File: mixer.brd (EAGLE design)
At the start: 23 x 40 mm, 21 parts, among them U2 SA602AD8-SOIC

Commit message: updating layouts and parts
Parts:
- moved JP1 0.64 mm to (11.5, 3.17)
- moved R4 0.25 mm to (1.91, 7.11)
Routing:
- net GND: track 117.4 -> 0.00 mm
- net N$5: track 56.3 -> 35.7 mm, vias 0 -> 1
- net ANT_OUT: track 42.9 -> 29.7 mm, vias 1 -> 0
- net N$1: track 6.50 -> 17.9 mm
- net N$2: track 7.98 -> 17.6 mm
- net OUT_A: track 14.4 -> 18.6 mm, vias 0 -> 1
- net N$4: track 13.6 -> 15.3 mm, vias 0 -> 1
- net N$16: track 19.8 -> 21.5 mm, vias 2 -> 0
- net 6V_DC: track 27.5 -> 28.7 mm
- net ANT_IN: track 22.3 -> 23.5 mm
- net OUT_B: track 13.1 -> 12.3 mm

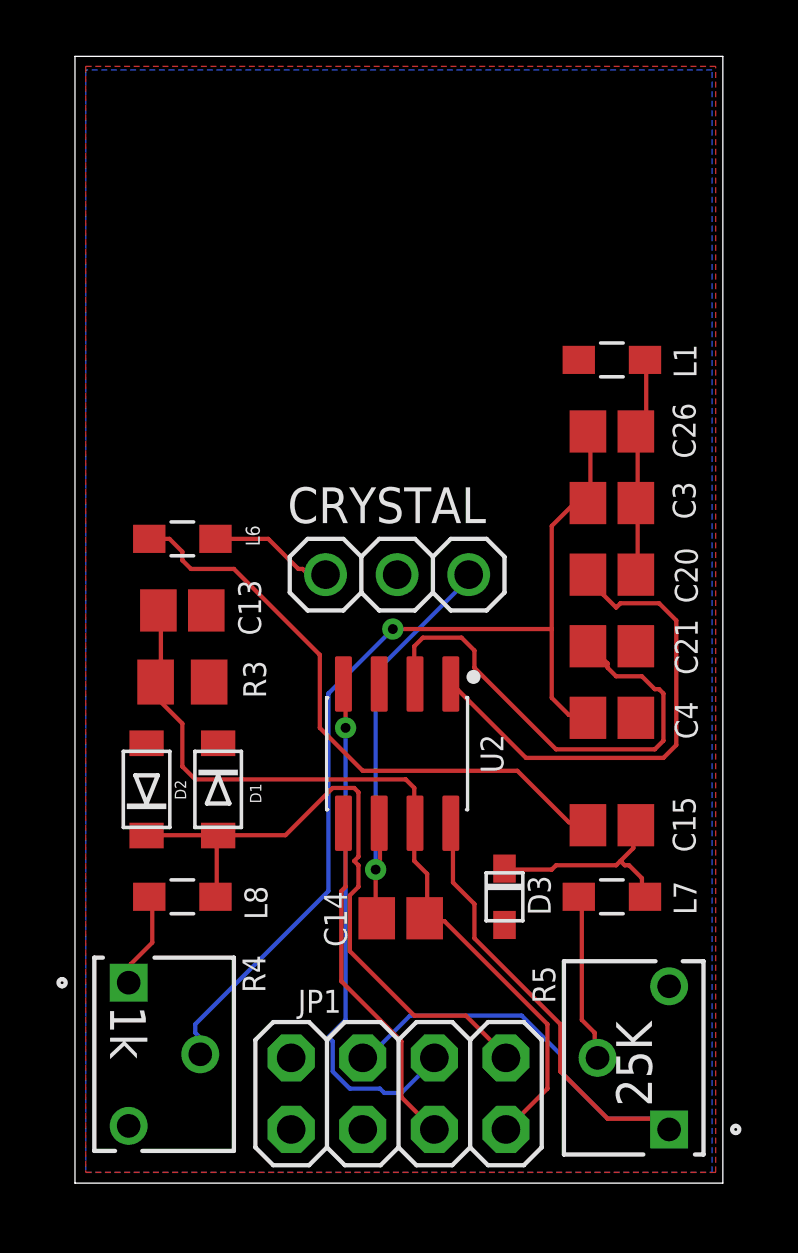
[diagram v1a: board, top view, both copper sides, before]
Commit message: cleaned up boards, new screenshots
Cleaned up the orientation and text on the boards. Ran them through the OshPark rules, and sent off v1 to get printed
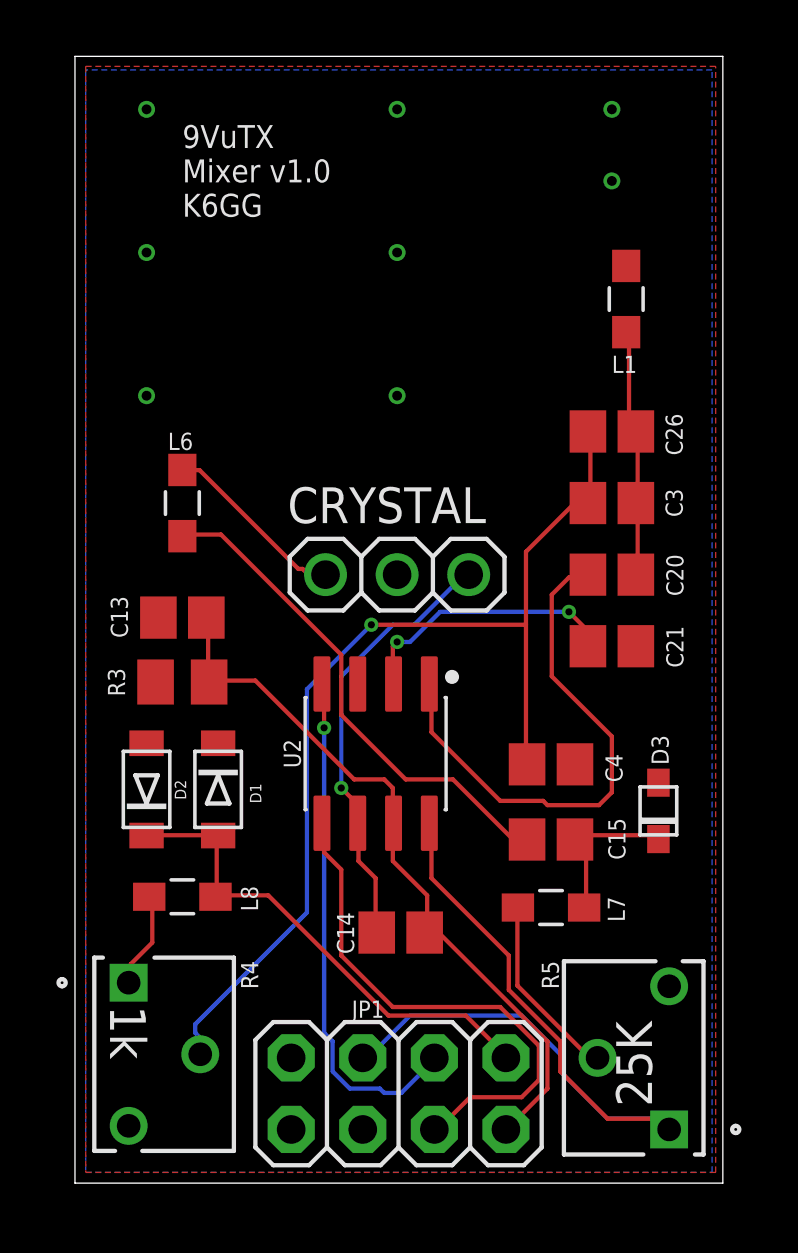
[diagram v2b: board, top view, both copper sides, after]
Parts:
- moved D3 6.25 mm to (20.7, 13.2), turned to 270 degrees
- moved C4 2.72 mm to (16.9, 14.9)
- moved C15 2.22 mm to (16.9, 12.2)
- moved L1 2.22 mm to (19.6, 31.4), turned to 270 degrees
- moved L7 2.19 mm to (16.9, 9.78)
- moved L6 1.27 mm to (3.81, 24.1), turned to 90 degrees
- moved U2 0.76 mm to (10.7, 15.2)
- moved C14 0.51 mm to (11.6, 8.89)
- moved C13 0.25 mm to (3.81, 20.1), turned to 180 degrees
- turned R3 to 0 degrees
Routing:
- net N$2: track 17.6 -> 9.63 mm, vias 0 -> 2
- net OUT_B: track 12.3 -> 19.0 mm
- net ANT_IN: track 23.5 -> 17.4 mm
- net ANT_OUT: track 29.7 -> 25.8 mm
- net N$16: track 21.5 -> 18.0 mm
- net N$15: track 4.43 -> 6.62 mm
- net N$17: track 7.53 -> 6.09 mm
- net N$3: track 7.90 -> 8.99 mm
- net N$1: track 17.9 -> 18.9 mm
- net N$5: track 35.7 -> 36.5 mm
- net N$18: track 5.99 -> 6.69 mm
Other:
- board text added: "9VuTX Mixer v1.0 K6GG"

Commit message: Updated boarts to v1.1
9VuTX Version 1.1

Several adjustments after mockup with V 1.0 of the board. That first version would be non-functional due to a few layout mismatches.

* fixed 2nd transistor layout to actually match part / spec (TO-252)
* rotated potentiometers 180 degrees so they face outward instead toward the middle of the board
* expanded pads of L2 (450uH inductor) to match recommended spec
* replaced phone jack with a true surface mount version (SJ-3523-SMT-TR)
* re-arranged the IO board to allow for the different phone jack
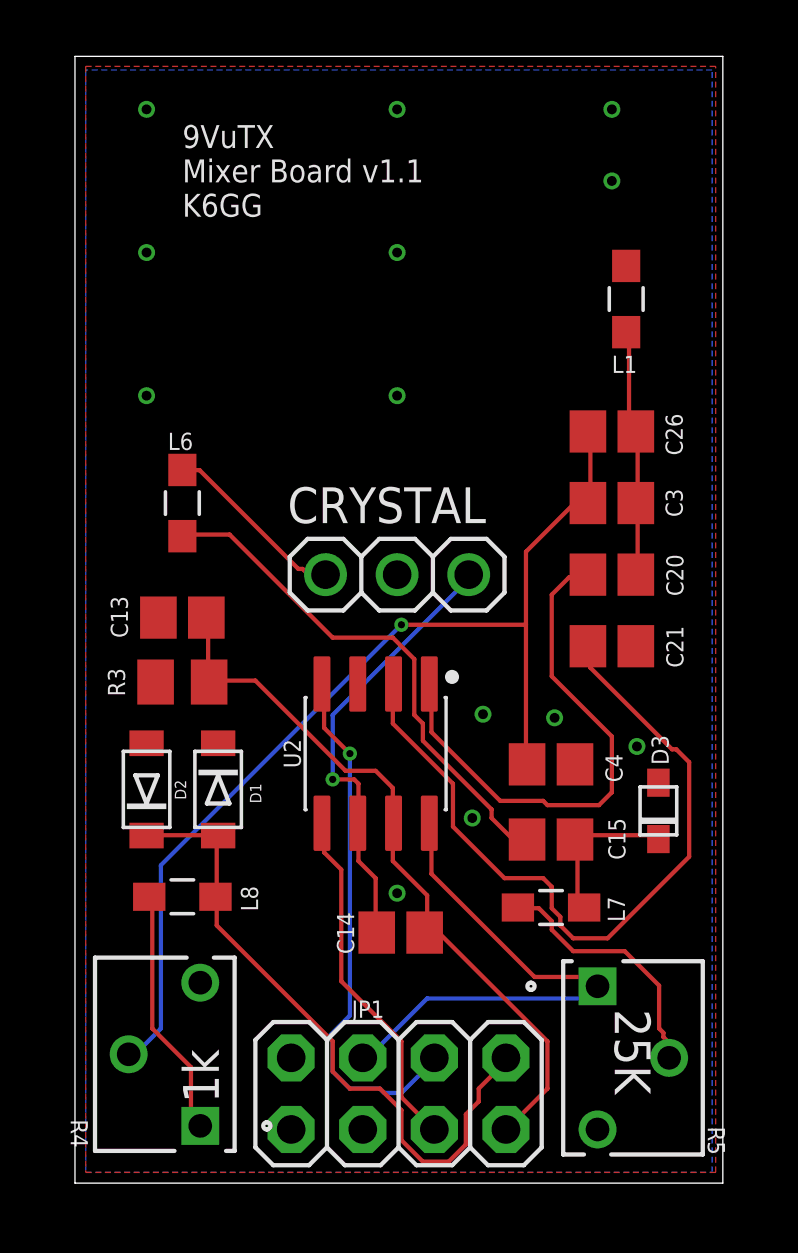
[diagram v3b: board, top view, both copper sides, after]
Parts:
- moved R4 5.68 mm to (4.45, 2.03), turned to 90 degrees
- moved R5 5.68 mm to (18.5, 6.99), turned to 270 degrees
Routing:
- net N$2: track 9.63 -> 27.7 mm, vias 2 -> 0
- net 6V_DC: track 29.1 -> 18.8 mm
- net OUT_B: track 19.0 -> 12.5 mm
- net ANT_IN: track 17.4 -> 23.4 mm
- net N$6: track 3.45 -> 8.87 mm
- net N$18: track 6.69 -> 9.06 mm
- net OUT_A: track 18.5 -> 19.1 mm
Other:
- board text added: "9VuTX Mixer Board v1.1 K6GG"
- board text removed: "9VuTX Mixer v1.0 K6GG"

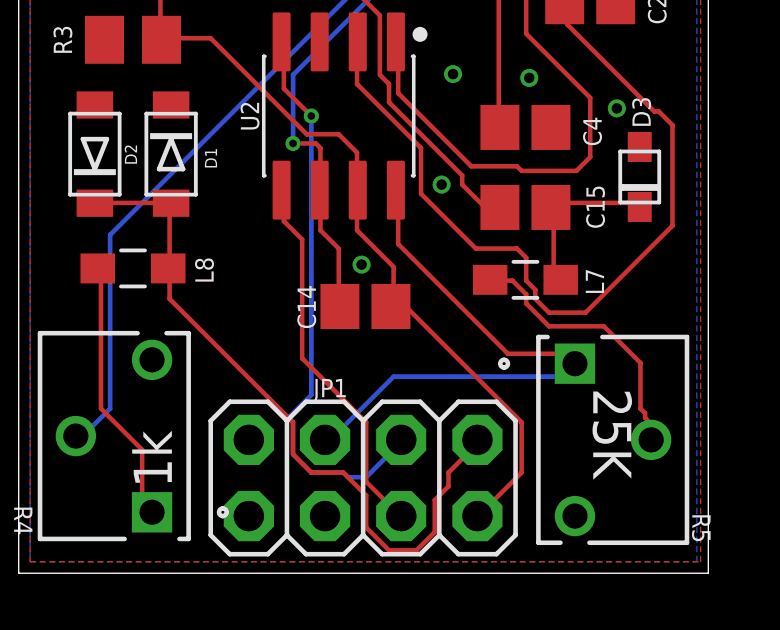
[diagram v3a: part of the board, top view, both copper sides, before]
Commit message: continuing on v 1.1
* removed "label" label from SMA connector
* increased the width of some lines likely to carry higher current
* attempted to clean up some little stuff
* updated images
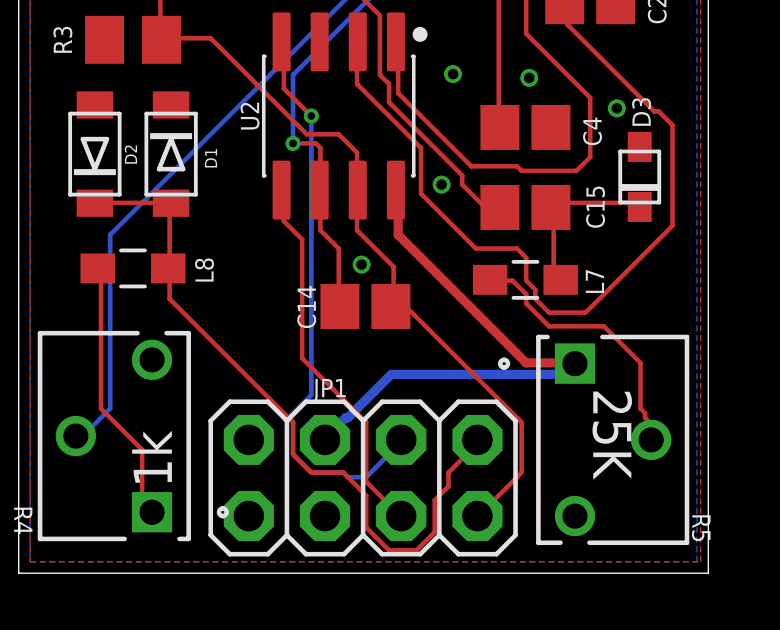
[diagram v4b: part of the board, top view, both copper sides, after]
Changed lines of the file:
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@@
 <class number="0" name="default" width="0" drill="0">
+</class>
+<class number="1" name="power" width="0.3048" drill="0">
 </class>
 </classes>
@@
 <via x="14.097" y="12.954" extent="1-16" drill="0.35"/>
 </signal>
-<signal name="6V_DC">
+<signal name="6V_DC" class="1">
 <contactref element="U2" pad="8"/>
 <contactref element="R5" pad="1"/>
 <contactref element="JP1" pad="5"/>
-<wire x1="12.6492" y1="10.9728" x2="12.6492" y2="12.6492" width="0.1524" layer="1"/>
-<wire x1="16.3068" y1="7.3152" x2="12.6492" y2="10.9728" width="0.1524" layer="1"/>
-<wire x1="18.1356" y1="7.3152" x2="16.3068" y2="7.3152" width="0.1524" layer="1"/>
-<wire x1="18.4404" y1="7.0104" x2="18.1356" y2="7.3152" width="0.1524" layer="1"/>
-<wire x1="12.6492" y1="12.6492" x2="12.573" y2="12.7699" width="0.1524" layer="1"/>
-<wire x1="18.4404" y1="7.0104" x2="18.542" y2="6.985" width="0.1524" layer="1"/>
-<wire x1="10.5156" y1="4.572" x2="10.2108" y2="4.572" width="0.1524" layer="16"/>
-<wire x1="12.4968" y1="6.5532" x2="10.5156" y2="4.572" width="0.1524" layer="16"/>
-<wire x1="18.1356" y1="6.5532" x2="12.4968" y2="6.5532" width="0.1524" layer="16"/>
-<wire x1="18.4404" y1="6.858" x2="18.1356" y2="6.5532" width="0.1524" layer="16"/>
-<wire x1="10.2108" y1="4.572" x2="10.2108" y2="4.445" width="0.1524" layer="16"/>
-<wire x1="18.4404" y1="6.858" x2="18.542" y2="6.985" width="0.1524" layer="16"/>
+<wire x1="12.6492" y1="11.2776" x2="12.6492" y2="12.573" width="0.3048" layer="1"/>
+<wire x1="16.9164" y1="7.0104" x2="12.6492" y2="11.2776" width="0.3048" layer="1"/>
+<wire x1="18.5166" y1="7.0104" x2="16.9164" y2="7.0104" width="0.3048" layer="1"/>
+<wire x1="12.6492" y1="12.573" x2="12.573" y2="12.7699" width="0.3048" layer="1"/>
+<wire x1="18.5166" y1="7.0104" x2="18.542" y2="6.985" width="0.3048" layer="1"/>
+<wire x1="10.8966" y1="5.1816" x2="10.2108" y2="4.4958" width="0.3048" layer="16"/>
+<wire x1="10.9728" y1="5.1816" x2="10.8966" y2="5.1816" width="0.3048" layer="16"/>
+<wire x1="12.4206" y1="6.6294" x2="10.9728" y2="5.1816" width="0.3048" layer="16"/>
+<wire x1="18.2118" y1="6.6294" x2="12.4206" y2="6.6294" width="0.3048" layer="16"/>
+<wire x1="18.5166" y1="6.9342" x2="18.2118" y2="6.6294" width="0.3048" layer="16"/>
+<wire x1="10.2108" y1="4.4958" x2="10.2108" y2="4.445" width="0.3048" layer="16"/>
+<wire x1="18.5166" y1="6.9342" x2="18.542" y2="6.985" width="0.3048" layer="16"/>
 </signal>
 <signal name="N$1">
@@
 <wire x1="21.0312" y1="4.572" x2="21.082" y2="4.445" width="0.1524" layer="1"/>
 </signal>
-<signal name="VIN">
+<signal name="VIN" class="1">
 <contactref element="JP1" pad="7"/>
 </signal>

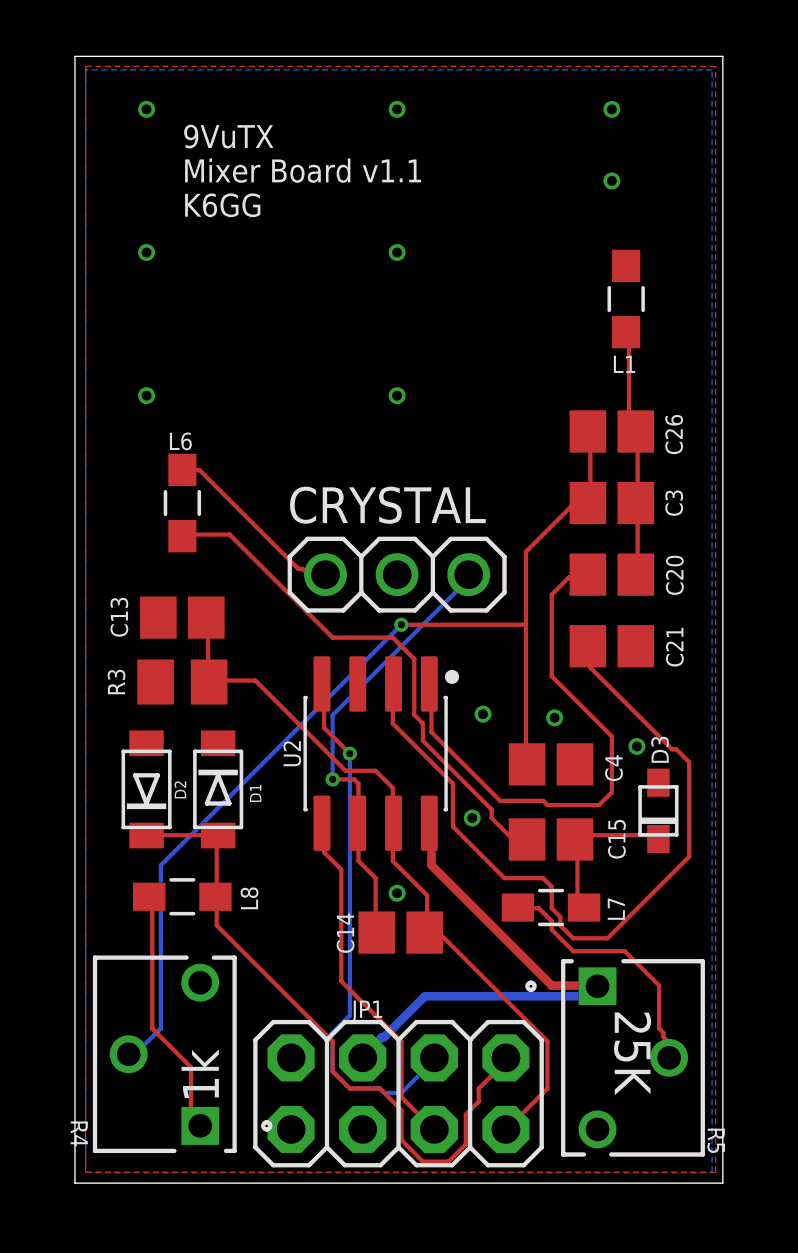
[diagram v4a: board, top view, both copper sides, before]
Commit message: Mixer board to 1.1a
Realized the jumper on the Mixer board was not oriented correctly. Unfortunately already ordered some of the previous version, so this is a new version.
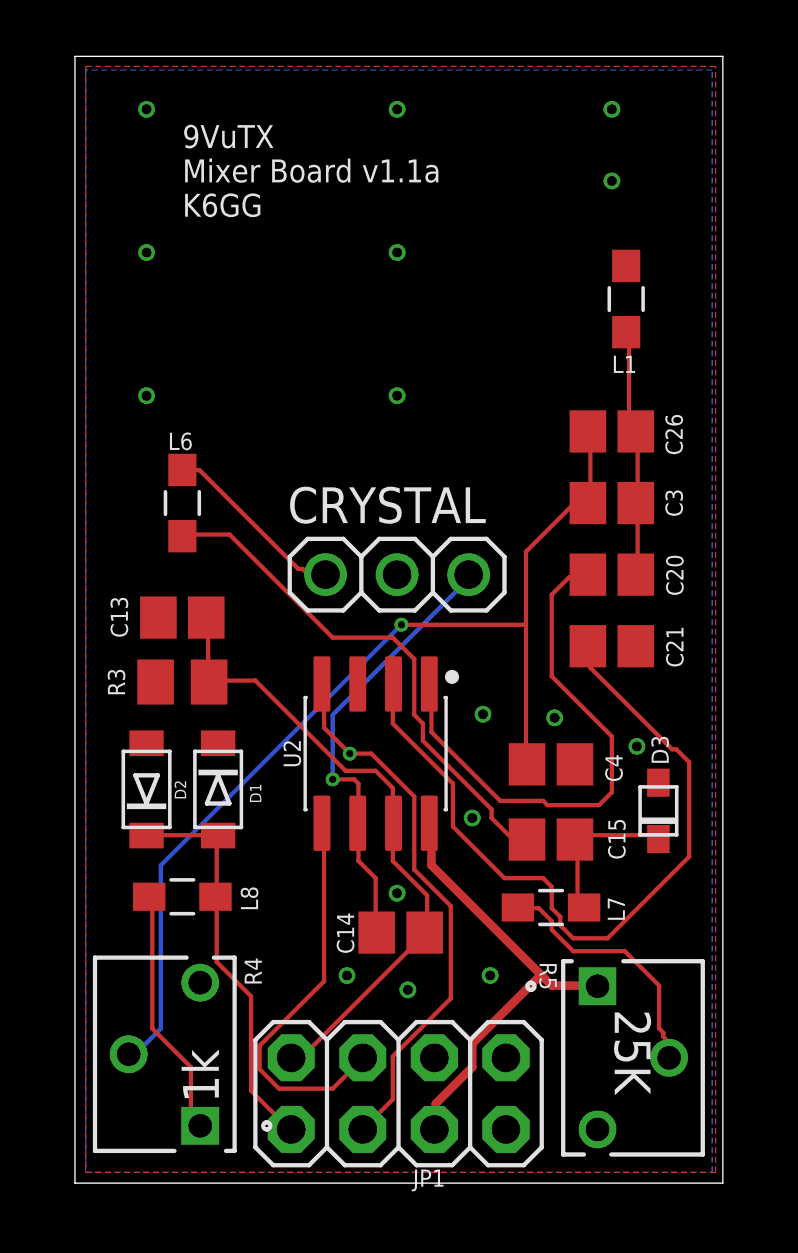
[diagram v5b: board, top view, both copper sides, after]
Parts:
- turned JP1 to 0 degrees
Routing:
- net ANT_IN: track 23.4 -> 14.1 mm
- net ANT_OUT: track 25.8 -> 23.3 mm
- net 6V_DC: track 18.6 -> 16.3 mm
- net OUT_B: track 12.5 -> 14.2 mm
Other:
- board text added: "9VuTX Mixer Board v1.1a K6GG"
- board text removed: "9VuTX Mixer Board v1.1 K6GG"
